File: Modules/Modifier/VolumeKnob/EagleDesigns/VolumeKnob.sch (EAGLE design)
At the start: 7 parts, among them U1 TINY85-20-DIP

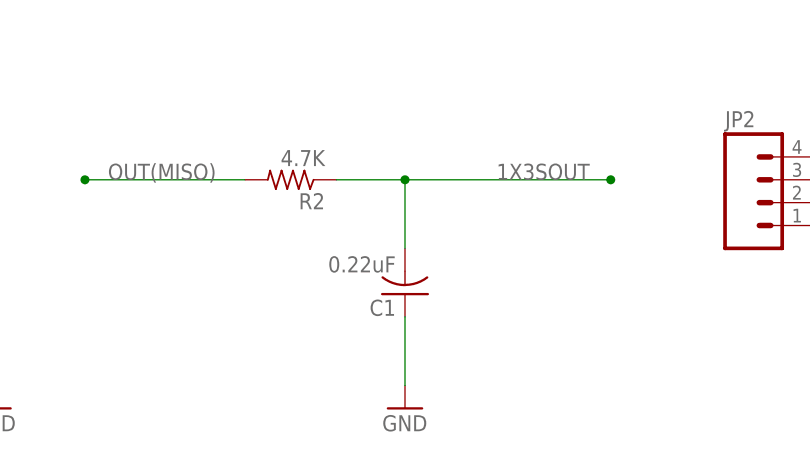
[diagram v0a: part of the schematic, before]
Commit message: changed 0403 cap to 0603 SMD cap
to solder without difficulty!
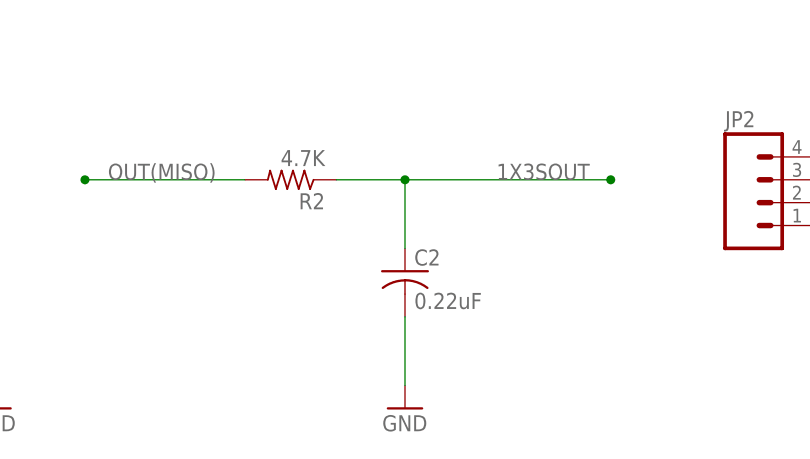
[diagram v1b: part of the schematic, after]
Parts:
- removed C1: 0.22uF, adafruit:C-USC0402
- added C2: 0.22uF, adafruit:C-USC0603
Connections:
- net 1X3SOUT: now also C2.1; no longer C1.2
- net GND: now also C2.2; no longer C1.1
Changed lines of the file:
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@@
 <part name="R1" library="adafruit" deviceset="R-US_" device="R0603" value="1M"/>
 <part name="R2" library="adafruit" deviceset="R-US_" device="R0603" value="4.7K"/>
-<part name="C1" library="adafruit" deviceset="C-US" device="C0402" value="0.22uF"/>
+<part name="C2" library="adafruit" deviceset="C-US" device="C0603" value="0.22uF"/>
 </parts>
 <sheets>
@@
 <instance part="R1" gate="G$1" x="50.8" y="-5.08" rot="R90"/>
 <instance part="R2" gate="G$1" x="190.5" y="7.62" rot="R180"/>
-<instance part="C1" gate="G$1" x="203.2" y="-5.08" rot="R180"/>
+<instance part="C2" gate="G$1" x="203.2" y="-2.54"/>
 </instances>
 <busses>
@@
 <wire x1="203.2" y1="-7.62" x2="203.2" y2="-15.24" width="0.1524" layer="91"/>
 <pinref part="GND3" gate="1" pin="GND"/>
-<pinref part="C1" gate="G$1" pin="1"/>
+<pinref part="C2" gate="G$1" pin="2"/>
 </segment>
 <segment>
@@
 <junction x="203.2" y="7.62"/>
 <pinref part="R2" gate="G$1" pin="1"/>
-<pinref part="C1" gate="G$1" pin="2"/>
+<pinref part="C2" gate="G$1" pin="1"/>
 </segment>
 </net>
